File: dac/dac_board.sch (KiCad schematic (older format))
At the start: 10 parts, among them J1 5-1814832-1, J2 5-1814832-1, J3 5-1814832-1, J4 5-1814832-1

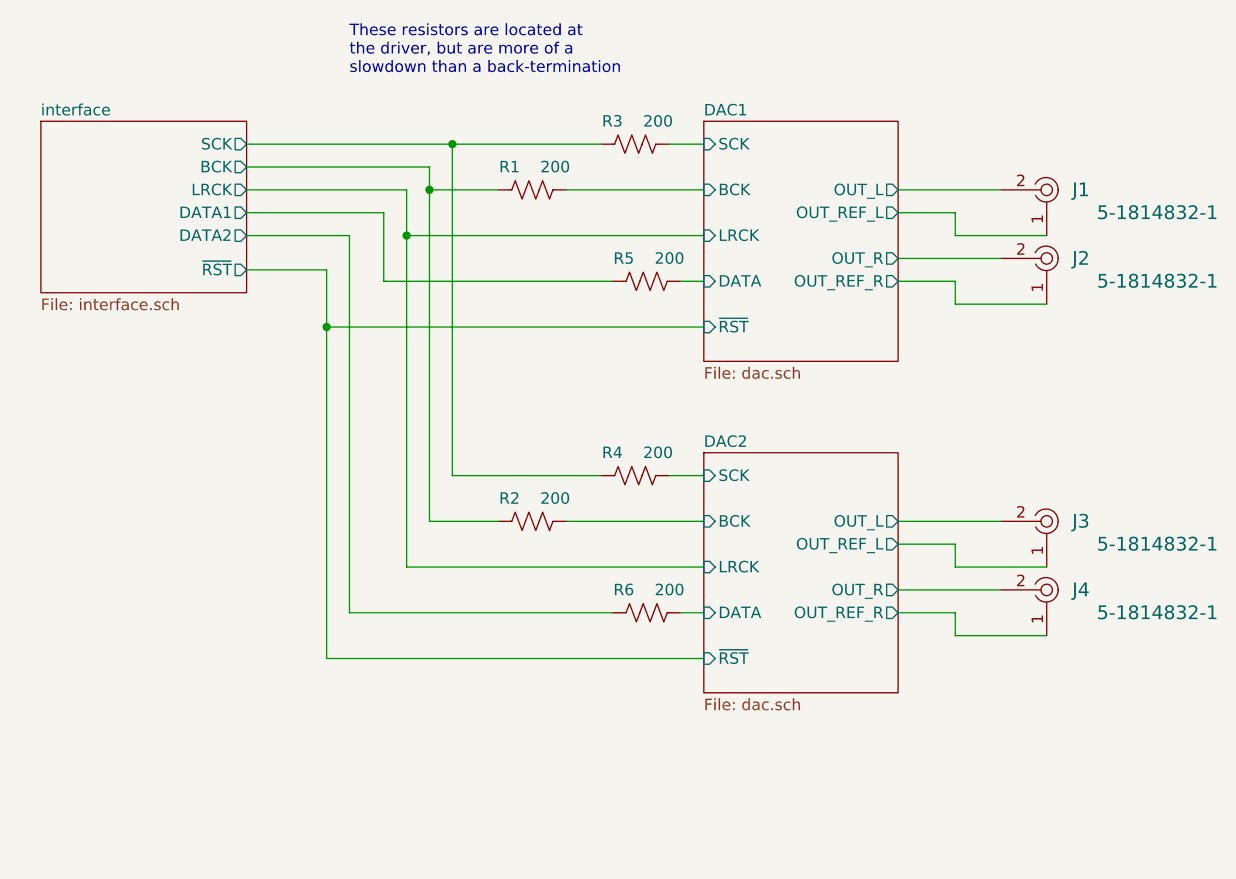
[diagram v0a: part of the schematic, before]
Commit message: DAC board is routed.  I also changed the digital interface to use a buffer (like I did on the input board) so that everything is buffered and we don't have multi-drop nets.
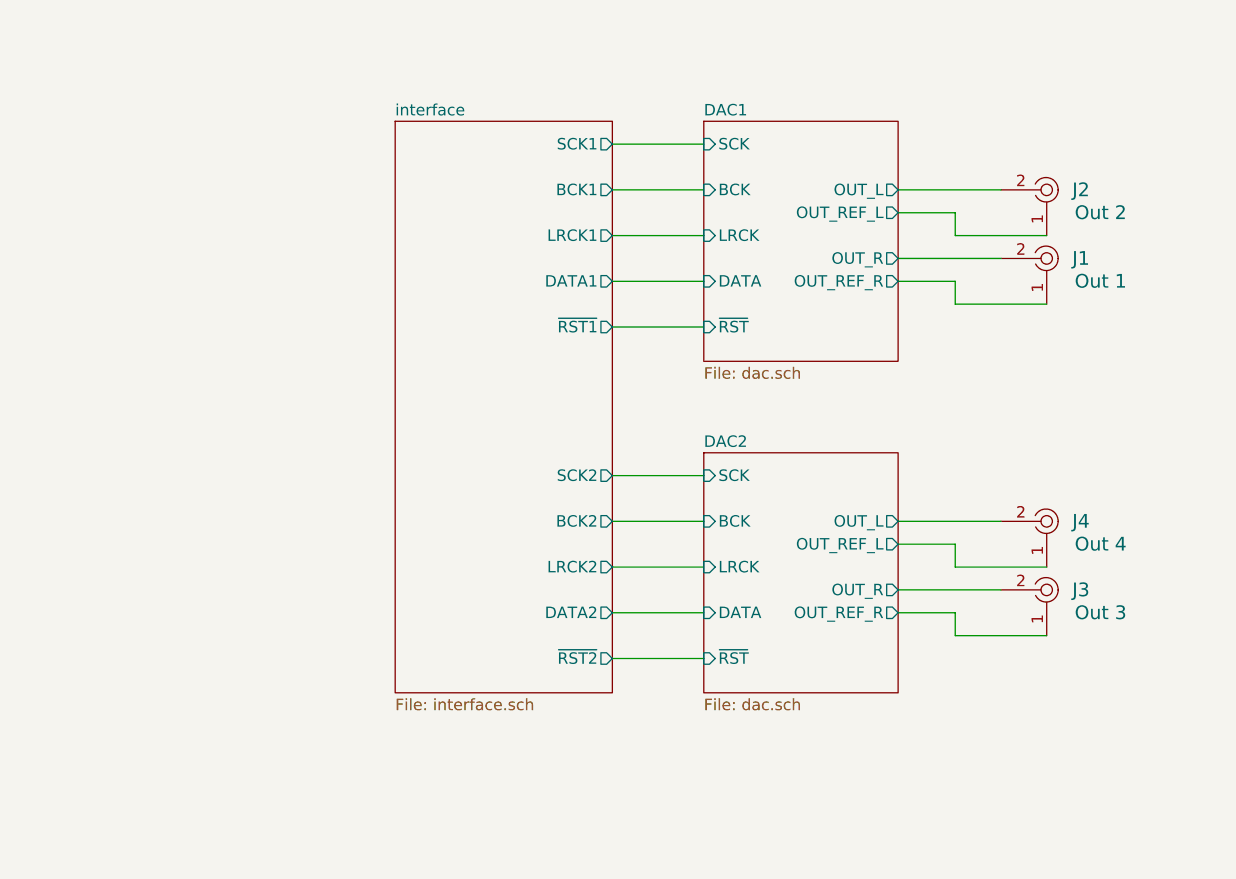
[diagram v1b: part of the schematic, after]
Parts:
- removed R1, R2, R3, R4, R5, R6: 200, Resistor_SMD:R_0603_1608Metric, symbol Device:R_US
- J1: value 5-1814832-1 -> Out 1
- J2: value 5-1814832-1 -> Out 2
- J3: value 5-1814832-1 -> Out 3
- J4: value 5-1814832-1 -> Out 4
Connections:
- net DAC1/OUT_L: now also J2.2; no longer J1.2
- net DAC1/OUT_R: now also J1.2; no longer J2.2
- net DAC1/OUT_REF_L: now also J2.1; no longer J1.1
- net DAC1/OUT_REF_R: now also J1.1; no longer J2.1
- net DAC2/OUT_L: now also J4.2; no longer J3.2
- net DAC2/OUT_R: now also J3.2; no longer J4.2
- net DAC2/OUT_REF_L: now also J4.1; no longer J3.1
- net DAC2/OUT_REF_R: now also J3.1; no longer J4.1
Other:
- note removed: "These resistors are located at\nthe driver, but are more of a \nslowdown than a back-termination"
- moved on the sheet: J1, J2, J3, J4

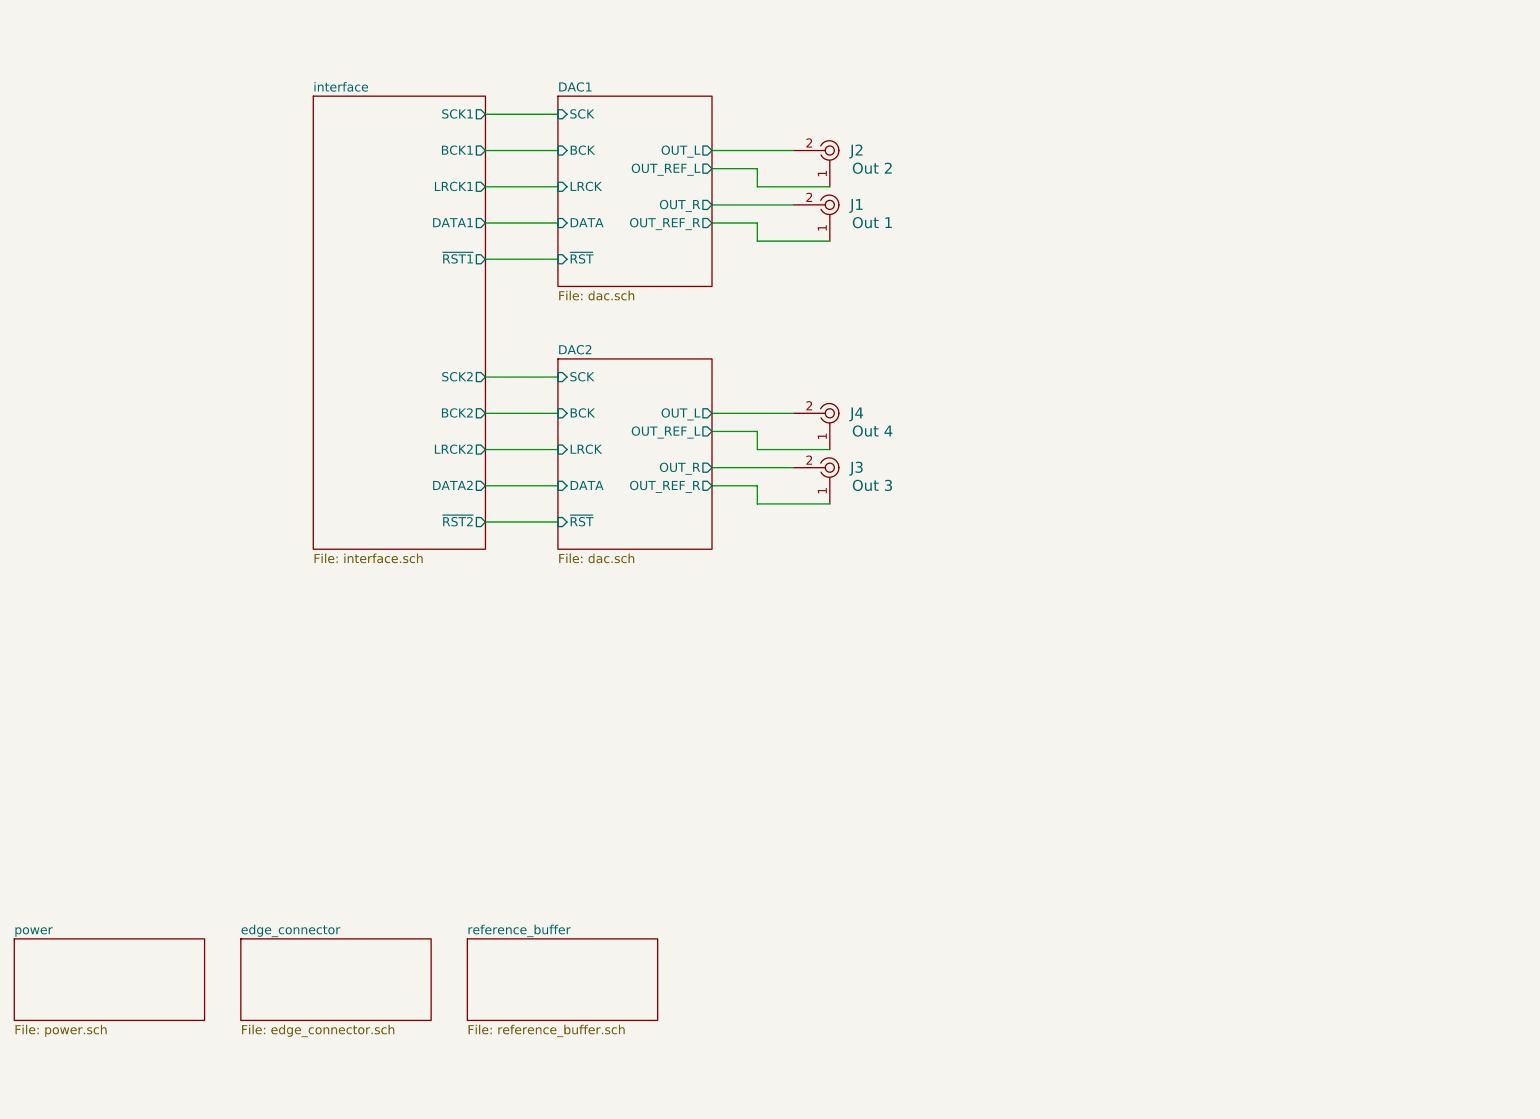
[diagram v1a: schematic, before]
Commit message: Everything seems ready to go for the DAC board.  Made my BOM and checked it twice. Checked footprints of new components and fixed J5, R7-R10.
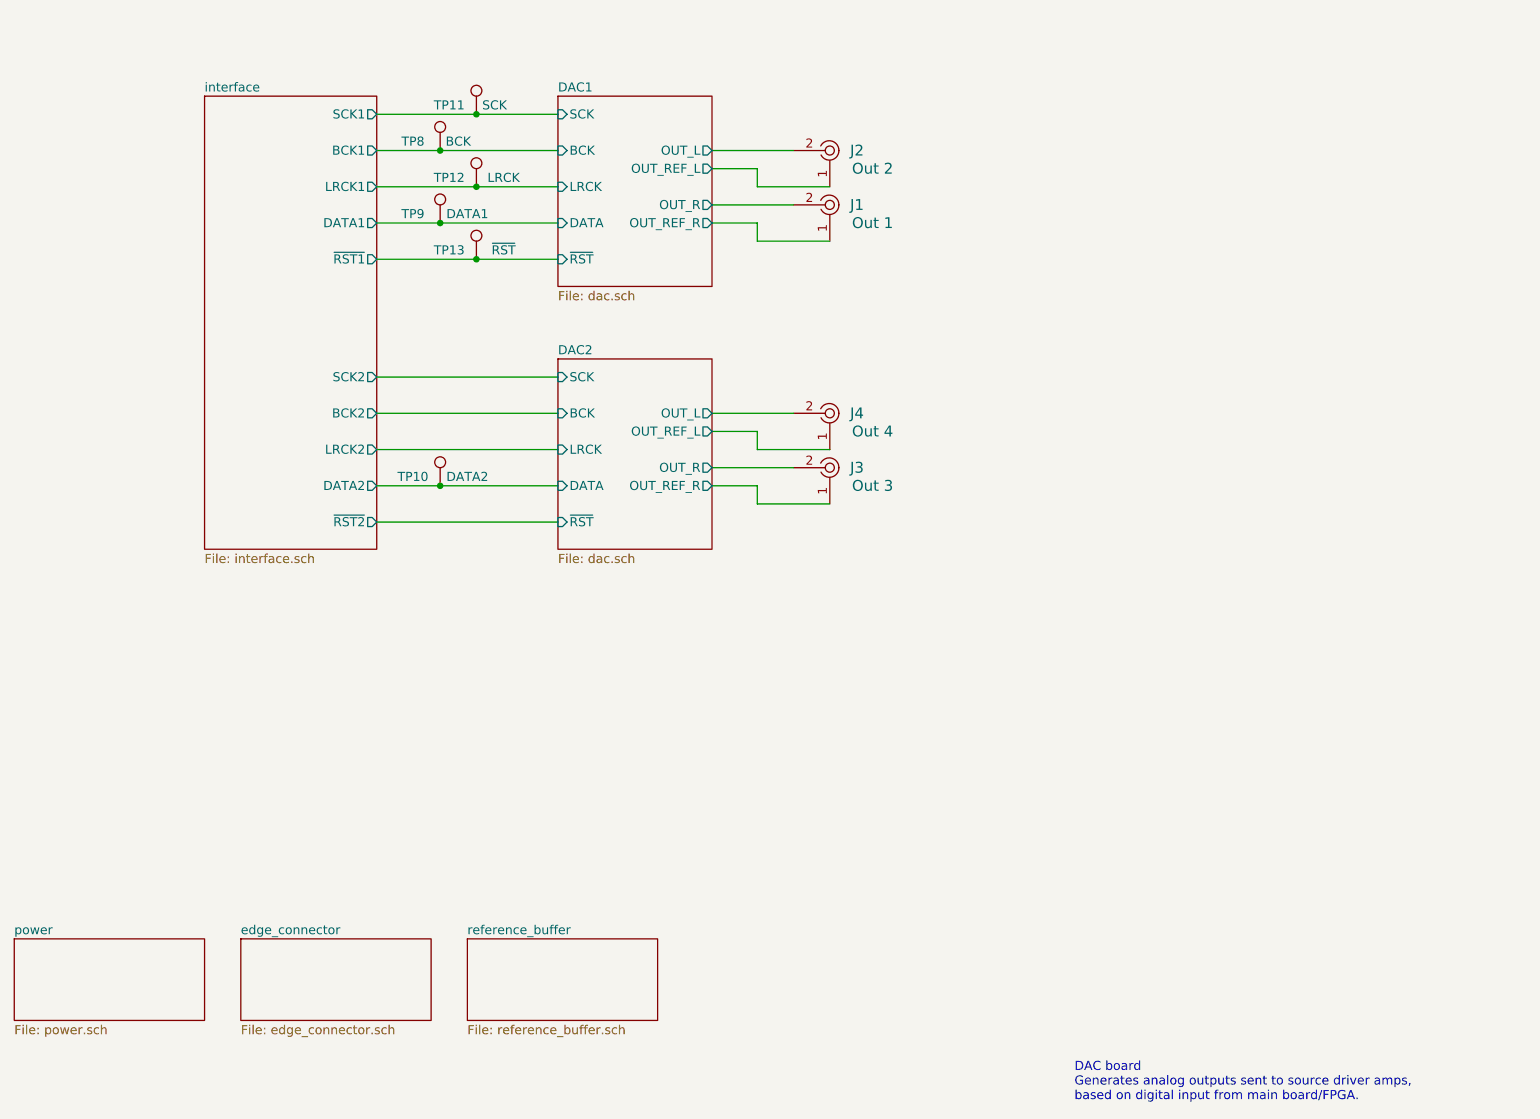
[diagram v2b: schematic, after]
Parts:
- added TP10: DATA2, TestPoint:TestPoint_THTPad_D1.5mm_Drill0.7mm, symbol Connector:TestPoint
- added TP11: SCK, TestPoint:TestPoint_THTPad_D1.5mm_Drill0.7mm, symbol Connector:TestPoint
- added TP12: LRCK, TestPoint:TestPoint_THTPad_D1.5mm_Drill0.7mm, symbol Connector:TestPoint
- added TP13: ~RST, TestPoint:TestPoint_THTPad_D1.5mm_Drill0.7mm, symbol Connector:TestPoint
- added TP8: BCK, TestPoint:TestPoint_THTPad_D1.5mm_Drill0.7mm, symbol Connector:TestPoint
- added TP9: DATA1, TestPoint:TestPoint_THTPad_D1.5mm_Drill0.7mm, symbol Connector:TestPoint
- J1, J2, J3, J4: DK line (none) -> D.29; Digikey (none) -> WM5543-ND; MPN 5-1814832-1 -> 0733910060
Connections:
- net DAC1/BCK: now also TP8.1
- net DAC1/DATA: now also TP9.1
- net DAC1/LRCK: now also TP12.1
- net DAC1/SCK: now also TP11.1
- net DAC1/~RST: now also TP13.1
- net DAC2/DATA: now also TP10.1
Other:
- note added: "DAC board\nGenerates analog outputs sent to source driver amps,\nbased on digital input from main board/FPGA."
